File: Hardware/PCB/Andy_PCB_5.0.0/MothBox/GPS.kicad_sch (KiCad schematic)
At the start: 10 parts, among them U1 Days, U17 GPs 5 pin PM2.54-1*5, U2 Hours1, U6 Hours2, U7 Modes, U8 CD74HC4067M96E4, U9 CD74HC4067M96E4

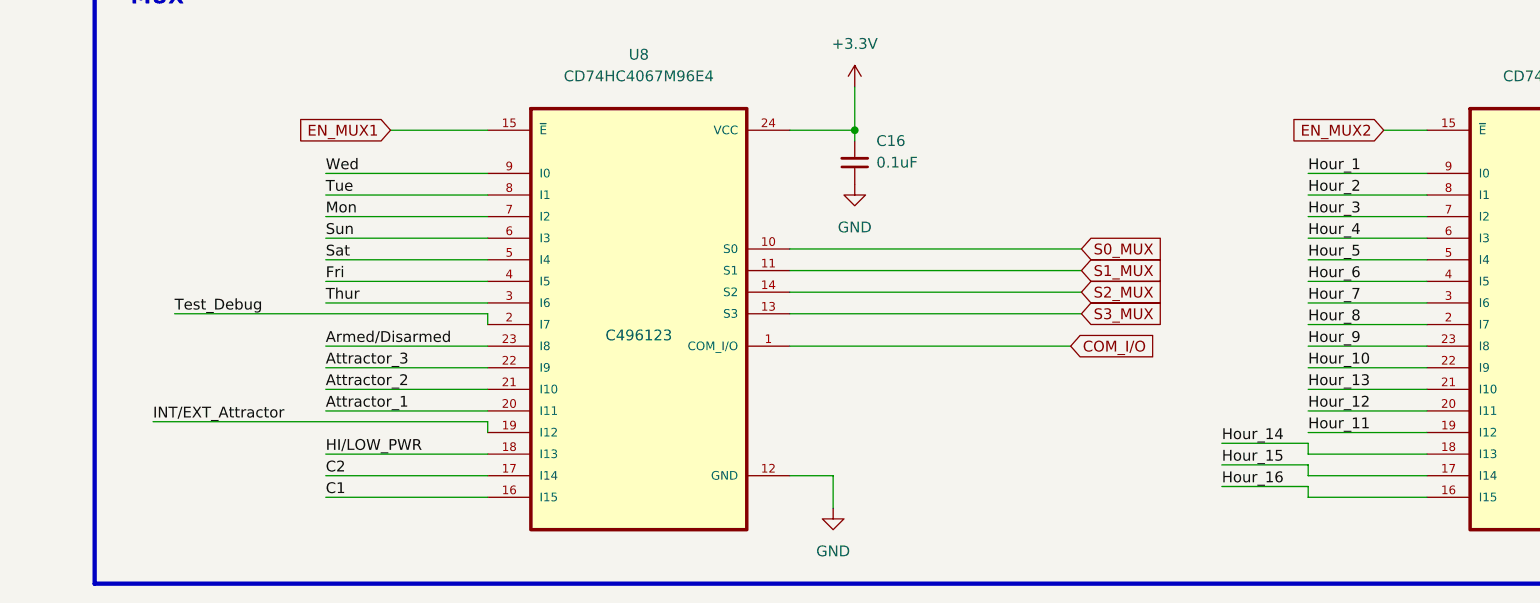
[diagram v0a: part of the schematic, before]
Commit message: Multiplexers wired together
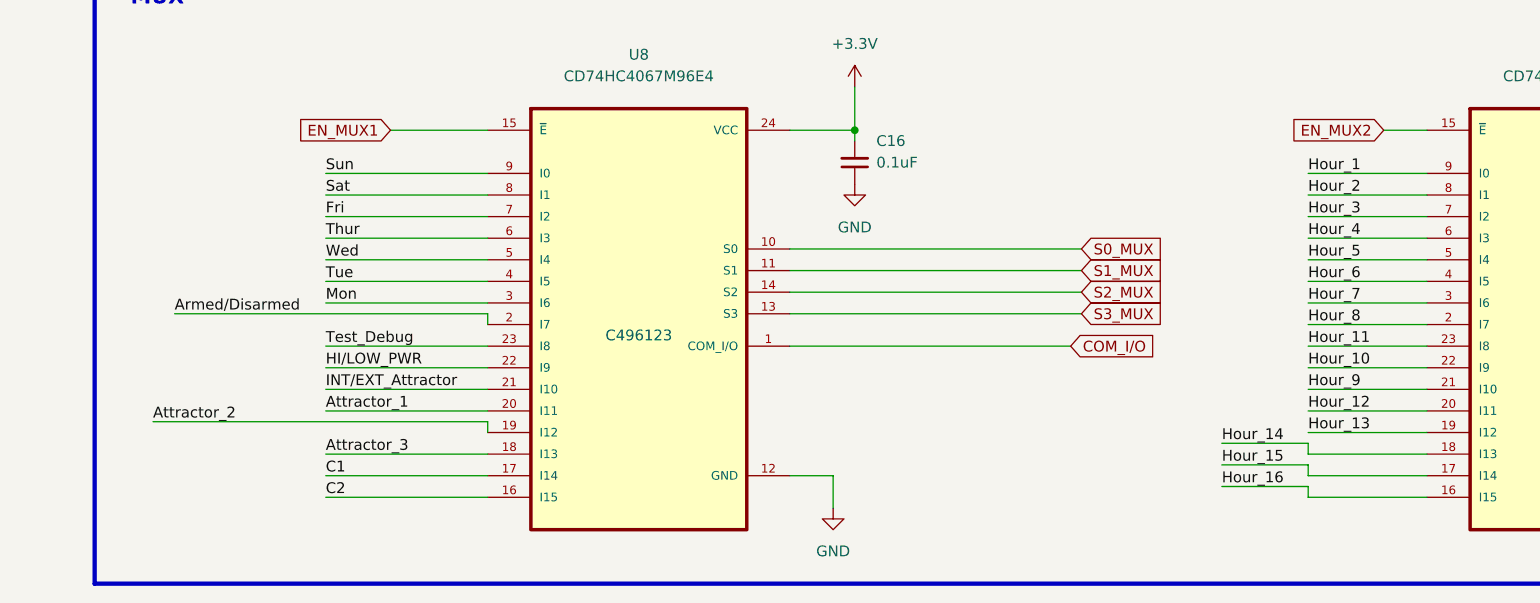
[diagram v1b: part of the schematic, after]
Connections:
- net Armed/Disarmed: now also U8.2 (I7); no longer U8.23 (I8)
- net Attractor_2: now also U8.19 (I12); no longer U8.21 (I10)
- net Attractor_3: now also U8.18 (I13); no longer U8.22 (I9)
- net C1: now also U8.17 (I14); no longer U8.16 (I15)
- net C2: now also U8.16 (I15); no longer U8.17 (I14)
- net Fri: now also U8.7 (I2); no longer U8.4 (I5)
- net HI/LOW_PWR: now also U8.22 (I9); no longer U8.18 (I13)
- net Hour_11: now also U9.23 (I8); no longer U9.19 (I12)
- net Hour_13: now also U9.19 (I12); no longer U9.21 (I10)
- net Hour_9: now also U9.21 (I10); no longer U9.23 (I8)
- net INT/EXT_Attractor: now also U8.21 (I10); no longer U8.19 (I12)
- net Mon: now also U8.3 (I6); no longer U8.7 (I2)
- net Sat: now also U8.8 (I1); no longer U8.5 (I4)
- net Sun: now also U8.9 (I0); no longer U8.6 (I3)
- net Test_Debug: now also U8.23 (I8); no longer U8.2 (I7)
- net Thur: now also U8.6 (I3); no longer U8.3 (I6)
- net Tue: now also U8.4 (I5); no longer U8.8 (I1)
- net Wed: now also U8.5 (I4); no longer U8.9 (I0)
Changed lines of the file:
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@@
 		)
 	)
-	(label "INT{slash}EXT_Attractor"
+	(label "Attractor_2"
 		(at 43.18 163.83 0)
 		(effects
@@
 		)
 	)
-	(label "Attractor_2"
+	(label "INT{slash}EXT_Attractor"
 		(at 63.5 160.02 0)
 		(effects
@@
 		)
 	)
-	(label "C1"
+	(label "C2"
 		(at 63.5 172.72 0)
 		(effects
@@
 		)
 	)
-	(label "Hour_9"
+	(label "Hour_11"
 		(at 179.07 154.94 0)
 		(effects
@@
 		)
 	)
-	(label "Thur"
+	(label "Mon"
 		(at 63.5 149.86 0)
 		(effects
@@
 		)
 	)
-	(label "Wed"
+	(label "Sun"
 		(at 63.5 134.62 0)
 		(effects
@@
 		)
 	)
-	(label "Armed{slash}Disarmed"
+	(label "Test_Debug"
 		(at 63.5 154.94 0)
 		(effects
@@
 		)
 	)
-	(label "C2"
+	(label "C1"
 		(at 63.5 170.18 0)
 		(effects
@@
 		)
 	)
-	(label "Hour_11"
+	(label "Hour_13"
 		(at 179.07 165.1 0)
 		(effects
@@
 		)
 	)
-	(label "Mon"
+	(label "Fri"
 		(at 63.5 139.7 0)
 		(effects
@@
 		)
 	)
-	(label "Fri"
+	(label "Tue"
 		(at 63.5 147.32 0)
 		(effects
@@
 		)
 	)
-	(label "Sun"
+	(label "Thur"
 		(at 63.5 142.24 0)
 		(effects
@@
 		)
 	)
-	(label "Sat"
+	(label "Wed"
 		(at 63.5 144.78 0)
 		(effects
@@
 		)
 	)
-	(label "Test_Debug"
+	(label "Armed{slash}Disarmed"
 		(at 45.72 151.13 0)
 		(effects
@@
 		)
 	)
-	(label "Attractor_3"
+	(label "HI{slash}LOW_PWR"
 		(at 63.5 157.48 0)
 		(effects
@@
 		)
 	)
-	(label "Hour_13"
+	(label "Hour_9"
 		(at 179.07 160.02 0)
 		(effects
@@
 		)
 	)
-	(label "HI{slash}LOW_PWR"
+	(label "Attractor_3"
 		(at 63.5 167.64 0)
 		(effects
@@
 		)
 	)
-	(label "Tue"
+	(label "Sat"
 		(at 63.5 137.16 0)
 		(effects

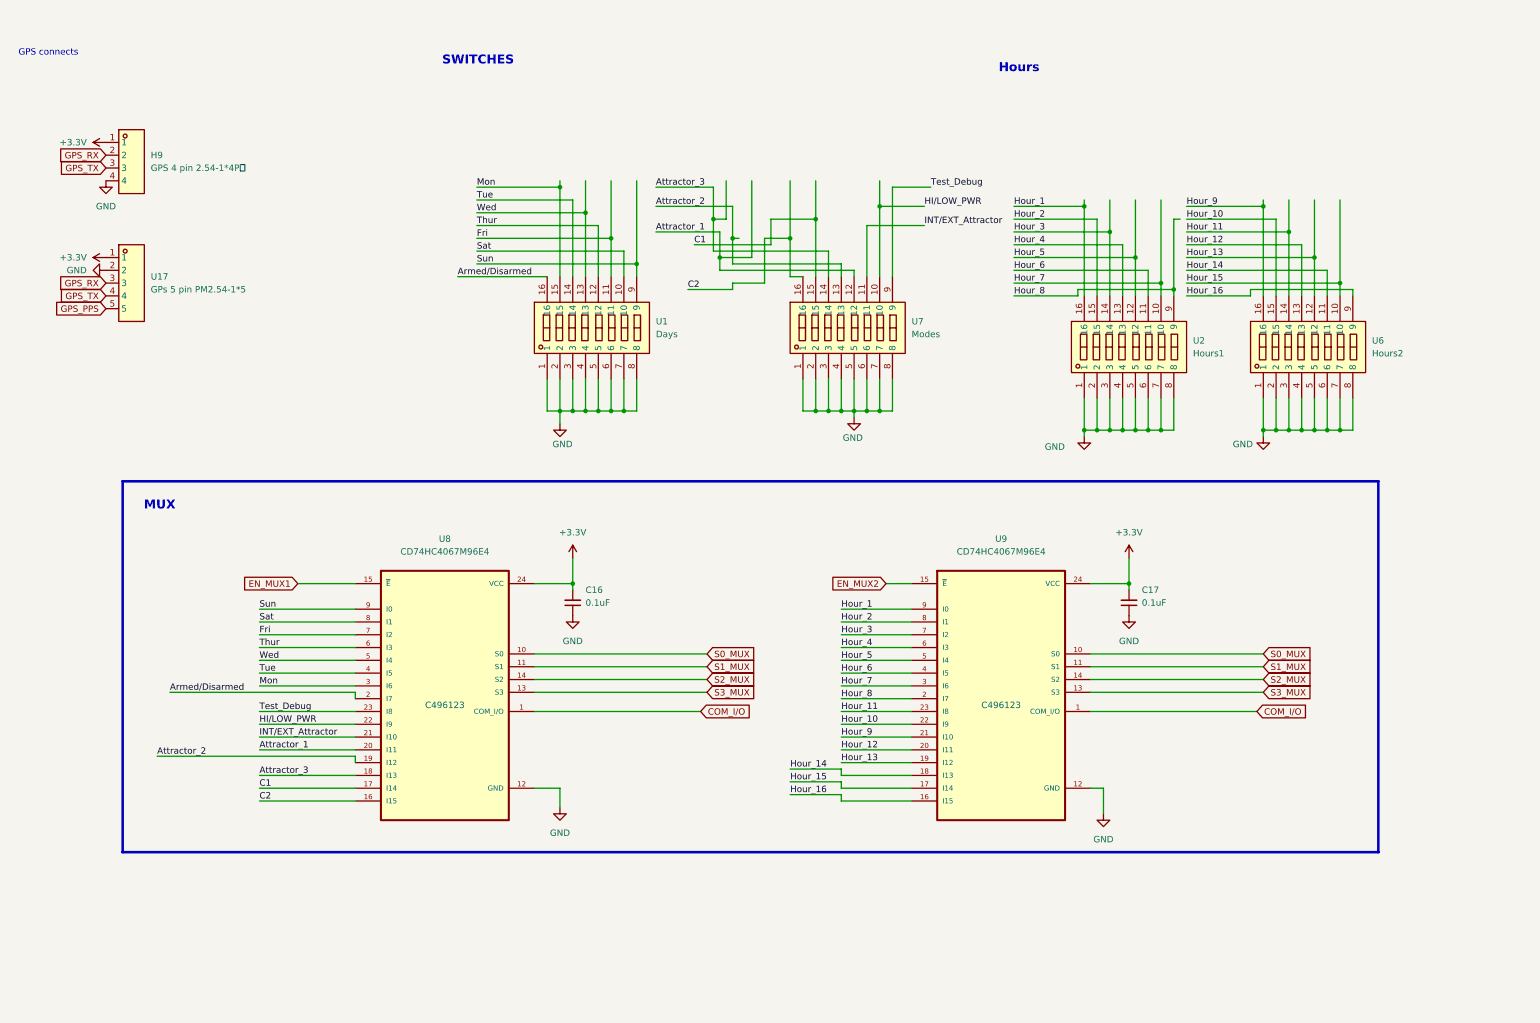
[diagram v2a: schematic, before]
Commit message: Switched from Analog Muxers to Shift Registers
Freed up 3 pins on the RasPi
Using 4 pins
SHIFT LOAD
SHIFT CLOCK
SHIFT DATA
SWITCH ENABLE
The Switch Enable pin drives +V to the switch array so it's not 'on' all the time

These hardware changes require changes to the code base
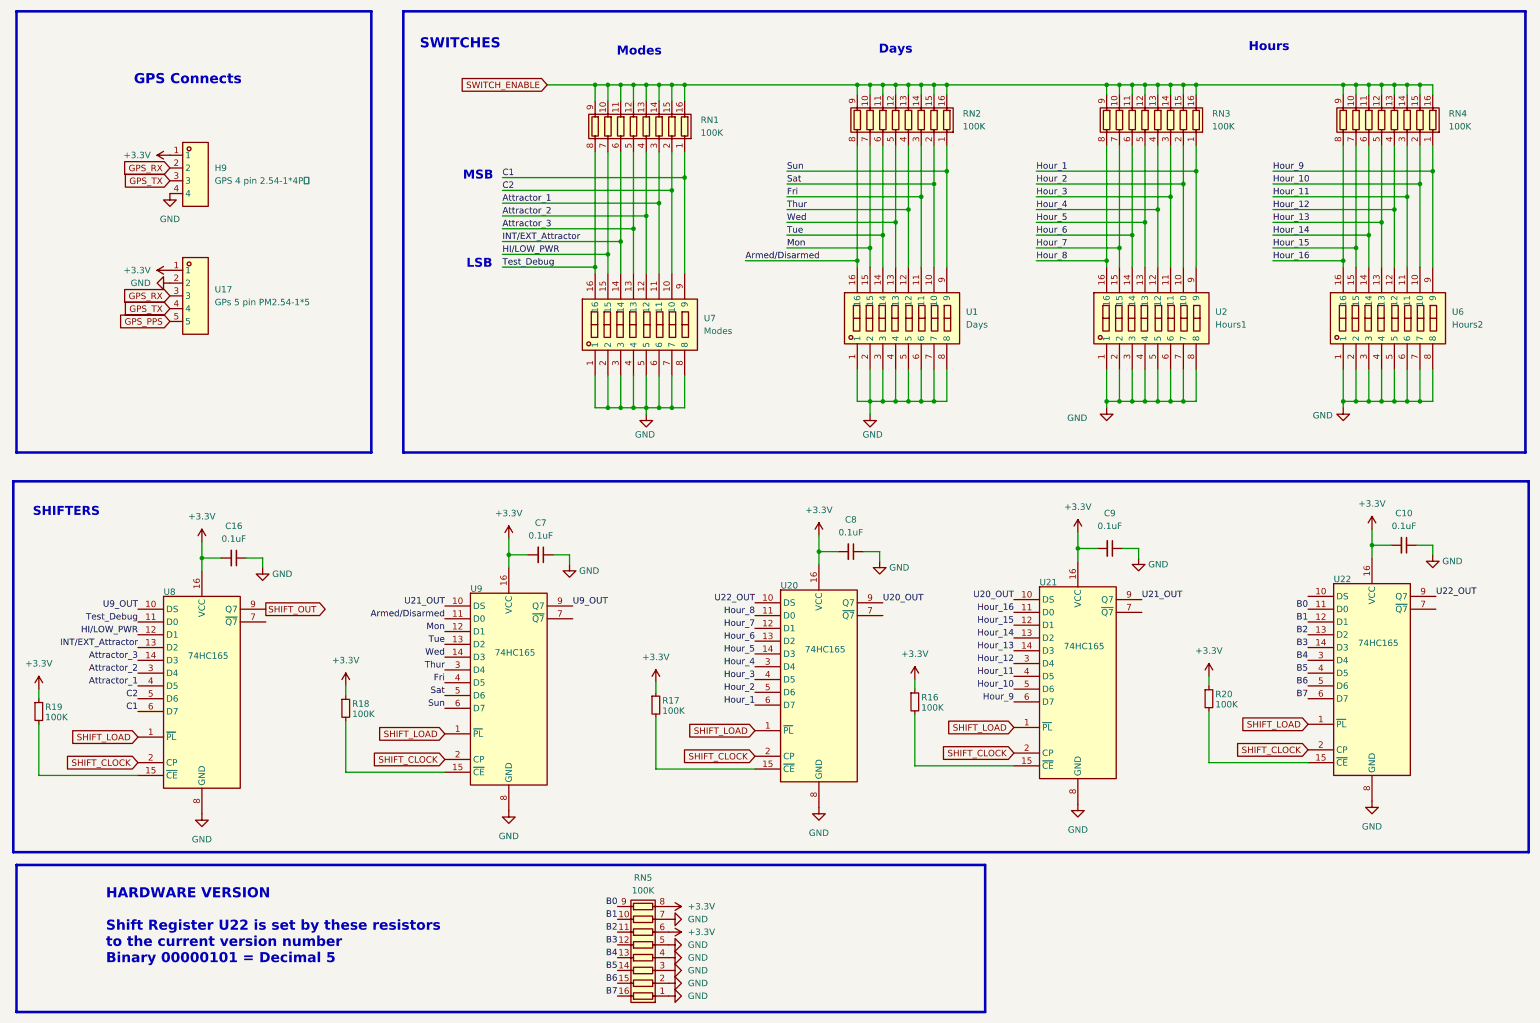
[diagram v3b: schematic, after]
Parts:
- removed C17: 0.1uF, Capacitor_SMD:C_0805_2012Metric, symbol Device:C_Small
- removed U8, U9: CD74HC4067M96E4, easyeda2kicad:SOIC-24_L15.4-W7.5-P1.27-LS10.3-BL, symbol CD74HC4067M96E4:CD74HC4067M96E4
- added C10, C7, C8, C9: 0.1uF, Capacitor_SMD:C_0805_2012Metric, symbol Device:C_Small
- added R16, R17, R18, R19, R20: 100K, Resistor_SMD:R_0603_1608Metric, symbol Device:R_Small
- added RN1, RN2, RN3, RN4, RN5: 100K, AQLibrary:16P8-R-Array, symbol Device:R_Pack08
- added U20, U21, U22, U8, U9: 74HC165, Package_SO:SOIC-16_3.9x9.9mm_P1.27mm, symbol 74xx:74HC165
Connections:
- net +3.3V: now also C10.2, C7.2, C8.2, C9.2, R16.1, R17.1, R18.1, R19.1, R20.1, RN5.6 (R6.1), RN5.8 (R8.1), U20.16 (VCC), U21.16 (VCC), U22.16 (VCC), U8.16 (VCC), U9.16 (VCC)
- net Armed/Disarmed: now also RN2.8 (R8.1), U9.11 (D0)
- net Attractor_1: now also U7.11, RN1.3 (R3.1), U8.4 (D5); no longer U7.12
- net Attractor_2: now also U7.12, RN1.4 (R4.1), U8.3 (D4); no longer U7.13
- net Attractor_3: now also U7.13, RN1.5 (R5.1), U8.14 (D3); no longer U7.14
- net C1: now also U7.9, RN1.1 (R1.1), U8.6 (D7); no longer U7.15
- net C2: now also U7.10, RN1.2 (R2.1), U8.5 (D6); no longer U7.16
- net Fri: now also RN2.3 (R3.1), U9.4 (D5)
- net GND: now also C10.1, C7.1, C8.1, C9.1, RN5.1 (R1.1), RN5.2 (R2.1), RN5.3 (R3.1), RN5.4 (R4.1), RN5.5 (R5.1), RN5.7 (R7.1), U20.8 (GND), U21.8 (GND), U22.8 (GND), U8.8 (GND), U9.8 (GND)
- net HI/LOW_PWR: now also U7.15, RN1.7 (R7.1), U8.12 (D1); no longer U7.10
- net Hour_1: now also U2.9, RN3.1 (R1.1), U20.6 (D7); no longer U2.16
- net Hour_10: now also U6.10, RN4.2 (R2.1), U21.5 (D6); no longer U6.15
- net Hour_11: now also U6.11, RN4.3 (R3.1), U21.4 (D5); no longer U6.14
- net Hour_12: now also U6.12, RN4.4 (R4.1), U21.3 (D4); no longer U6.13
- net Hour_13: now also U6.13, RN4.5 (R5.1), U21.14 (D3); no longer U6.12
- net Hour_14: now also U6.14, RN4.6 (R6.1), U21.13 (D2); no longer U6.11
- net Hour_15: now also U6.15, RN4.7 (R7.1), U21.12 (D1); no longer U6.10
- net Hour_16: now also U6.16, RN4.8 (R8.1), U21.11 (D0); no longer U6.9
- net Hour_2: now also U2.10, RN3.2 (R2.1), U20.5 (D6); no longer U2.15
- net Hour_3: now also U2.11, RN3.3 (R3.1), U20.4 (D5); no longer U2.14
- net Hour_4: now also U2.12, RN3.4 (R4.1), U20.3 (D4); no longer U2.13
- net Hour_5: now also U2.13, RN3.5 (R5.1), U20.14 (D3); no longer U2.12
- net Hour_6: now also U2.14, RN3.6 (R6.1), U20.13 (D2); no longer U2.11
- net Hour_7: now also U2.15, RN3.7 (R7.1), U20.12 (D1); no longer U2.10
- net Hour_8: now also U2.16, RN3.8 (R8.1), U20.11 (D0); no longer U2.9
- net Hour_9: now also U6.9, RN4.1 (R1.1), U21.6 (D7); no longer U6.16
- net INT/EXT_Attractor: now also U7.14, RN1.6 (R6.1), U8.13 (D2); no longer U7.11
- net Mon: now also RN2.7 (R7.1), U9.12 (D1)
- net Sat: now also RN2.2 (R2.1), U9.5 (D6)
- net Sun: now also RN2.1 (R1.1), U9.6 (D7)
- net Test_Debug: now also U7.16, RN1.8 (R8.1), U8.11 (D0); no longer U7.9
- net Thur: now also RN2.4 (R4.1), U9.3 (D4)
- net Tue: now also RN2.6 (R6.1), U9.13 (D2)
- net Wed: now also RN2.5 (R5.1), U9.14 (D3)
- new net: R19.2, U8.15 (~{CE})
- new net: R20.2, U22.15 (~{CE})
- new net: R18.2, U9.15 (~{CE})
- new net: R17.2, U20.15 (~{CE})
- new net: R16.2, U21.15 (~{CE})
- new net B0: RN5.9 (R8.2), U22.11 (D0)
- new net B1: RN5.10 (R7.2), U22.12 (D1)
- new net B2: RN5.11 (R6.2), U22.13 (D2)
- new net B3: RN5.12 (R5.2), U22.14 (D3)
- new net B4: RN5.13 (R4.2), U22.3 (D4)
- new net B5: RN5.14 (R3.2), U22.4 (D5)
- new net B6: RN5.15 (R2.2), U22.5 (D6)
- new net B7: RN5.16 (R1.2), U22.6 (D7)
- new net SHIFT_CLOCK: U20.2 (CP), U21.2 (CP), U22.2 (CP), U8.2 (CP), U9.2 (CP)
- new net SHIFT_LOAD: U20.1 (~{PL}), U21.1 (~{PL}), U22.1 (~{PL}), U8.1 (~{PL}), U9.1 (~{PL})
- new net SHIFT_OUT: U8.9 (Q7)
- new net SWITCH_ENABLE: RN1.10 (R7.2), RN1.11 (R6.2), RN1.12 (R5.2), RN1.13 (R4.2), RN1.14 (R3.2), RN1.15 (R2.2), RN1.16 (R1.2), RN1.9 (R8.2), RN2.10 (R7.2), RN2.11 (R6.2), RN2.12 (R5.2), RN2.13 (R4.2), RN2.14 (R3.2), RN2.15 (R2.2), RN2.16 (R1.2), RN2.9 (R8.2), RN3.10 (R7.2), RN3.11 (R6.2), RN3.12 (R5.2), RN3.13 (R4.2), RN3.14 (R3.2), RN3.15 (R2.2), RN3.16 (R1.2), RN3.9 (R8.2), RN4.10 (R7.2), RN4.11 (R6.2), RN4.12 (R5.2), RN4.13 (R4.2), RN4.14 (R3.2), RN4.15 (R2.2), RN4.16 (R1.2), RN4.9 (R8.2)
- new net U20_OUT: U20.9 (Q7), U21.10 (DS)
- new net U21_OUT: U21.9 (Q7), U9.10 (DS)
- new net U22_OUT: U20.10 (DS), U22.9 (Q7)
- new net U9_OUT: U8.10 (DS), U9.9 (Q7)
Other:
- note added: "Days"
- note added: "GPS Connects"
- note added: "HARDWARE VERSION Shift Register U22 is set by these resistors to the current version number Binary 00000101 = Decimal 5"
- note added: "LSB"
- note added: "MSB"
- note added: "Modes"
- note added: "SHIFTERS"
- note removed: "GPS connects"
- note removed: "MUX"
- moved on the sheet: C16, H9, U1, U17, U2, U6, U7
